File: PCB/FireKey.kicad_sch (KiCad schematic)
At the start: 76 parts, among them P1 Pad, P2 Pad, SW1 SW_MEC_4A, U1 Arduino_Pro_Micro_USB-C

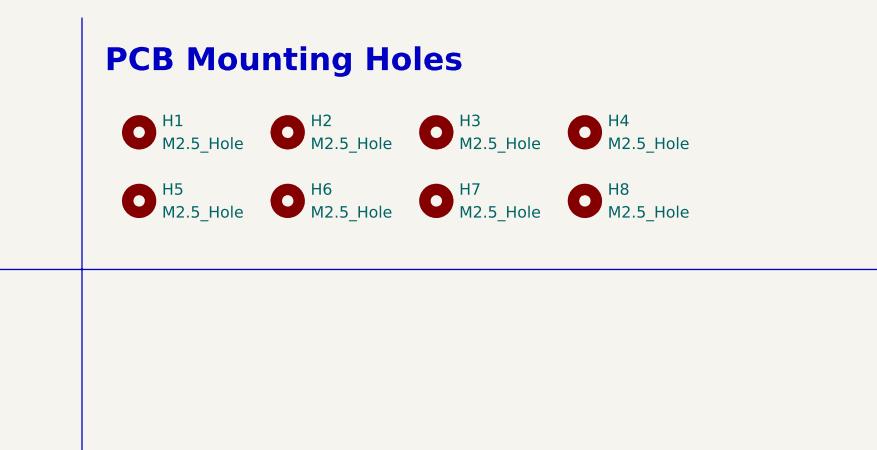
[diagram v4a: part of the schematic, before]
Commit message: deleted unused Mounting Holes in schematic
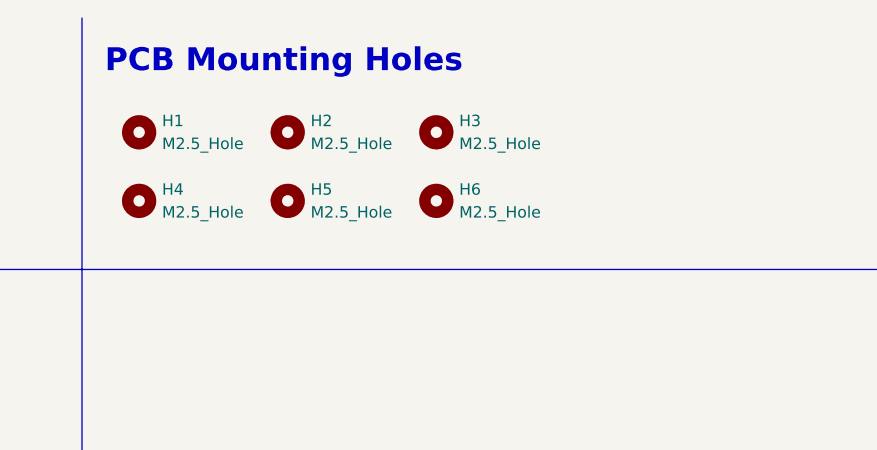
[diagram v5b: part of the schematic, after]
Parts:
- removed H7, H8: M2.5_Hole, MountingHole:MountingHole_2.7mm_M2.5, symbol Mechanical:MountingHole
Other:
- moved on the sheet: H4, H5, H6
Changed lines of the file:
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@@
     (pin "2")
   )
-  (symbol (lib_id "Mechanical:MountingHole") (at 194.31 33.02 0) (unit 1)
+  (symbol (lib_id "Mechanical:MountingHole") (at 210.82 33.02 0) (unit 1)
     (in_bom no) (on_board yes) (fields_autoplaced)
-    (property "Reference" "H5" (id 0) (at 196.85 31.7499 0)
-      (effects (font (size 1.27 1.27)) (justify left))
-    )
-    (property "Value" "M2.5_Hole" (id 1) (at 196.85 34.2899 0)
-      (effects (font (size 1.27 1.27)) (justify left))
-    )
-    (property "Footprint" "MountingHole:MountingHole_2.7mm_M2.5" (id 2) (at 194.31 33.02 0)
-      (effects (font (size 1.27 1.27)) hide)
-    )
-    (property "Datasheet" "-" (id 3) (at 194.31 33.02 0)
-      (effects (font (size 1.27 1.27)) hide)
-    )
-    (property "Part#" "-" (id 4) (at 194.31 33.02 0)
-      (effects (font (size 1.27 1.27)) hide)
-    )
-    (property "Supplier" "-" (id 5) (at 194.31 33.02 0)
+    (property "Reference" "H5" (id 0) (at 213.36 31.7499 0)
+      (effects (font (size 1.27 1.27)) (justify left))
+    )
+    (property "Value" "M2.5_Hole" (id 1) (at 213.36 34.2899 0)
+      (effects (font (size 1.27 1.27)) (justify left))
+    )
+    (property "Footprint" "MountingHole:MountingHole_2.7mm_M2.5" (id 2) (at 210.82 33.02 0)
+      (effects (font (size 1.27 1.27)) hide)
+    )
+    (property "Datasheet" "-" (id 3) (at 210.82 33.02 0)
+      (effects (font (size 1.27 1.27)) hide)
+    )
+    (property "Part#" "-" (id 4) (at 210.82 33.02 0)
+      (effects (font (size 1.27 1.27)) hide)
+    )
+    (property "Supplier" "-" (id 5) (at 210.82 33.02 0)
       (effects (font (size 1.27 1.27)) hide)
     )
@@
     (pin "4")
   )
-  (symbol (lib_id "Mechanical:MountingHole") (at 210.82 33.02 0) (unit 1)
+  (symbol (lib_id "Mechanical:MountingHole") (at 227.33 33.02 0) (unit 1)
     (in_bom no) (on_board yes) (fields_autoplaced)
-    (property "Reference" "H6" (id 0) (at 213.36 31.7499 0)
-      (effects (font (size 1.27 1.27)) (justify left))
-    )
-    (property "Value" "M2.5_Hole" (id 1) (at 213.36 34.2899 0)
-      (effects (font (size 1.27 1.27)) (justify left))
-    )
-    (property "Footprint" "MountingHole:MountingHole_2.7mm_M2.5" (id 2) (at 210.82 33.02 0)
-      (effects (font (size 1.27 1.27)) hide)
-    )
-    (property "Datasheet" "-" (id 3) (at 210.82 33.02 0)
-      (effects (font (size 1.27 1.27)) hide)
-    )
-    (property "Part#" "-" (id 4) (at 210.82 33.02 0)
-      (effects (font (size 1.27 1.27)) hide)
-    )
-    (property "Supplier" "-" (id 5) (at 210.82 33.02 0)
+    (property "Reference" "H6" (id 0) (at 229.87 31.7499 0)
+      (effects (font (size 1.27 1.27)) (justify left))
+    )
+    (property "Value" "M2.5_Hole" (id 1) (at 229.87 34.2899 0)
+      (effects (font (size 1.27 1.27)) (justify left))
+    )
+    (property "Footprint" "MountingHole:MountingHole_2.7mm_M2.5" (id 2) (at 227.33 33.02 0)
+      (effects (font (size 1.27 1.27)) hide)
+    )
+    (property "Datasheet" "-" (id 3) (at 227.33 33.02 0)
+      (effects (font (size 1.27 1.27)) hide)
+    )
+    (property "Part#" "-" (id 4) (at 227.33 33.02 0)
+      (effects (font (size 1.27 1.27)) hide)
+    )
+    (property "Supplier" "-" (id 5) (at 227.33 33.02 0)
       (effects (font (size 1.27 1.27)) hide)
     )
@@
     (pin "4")
   )
-  (symbol (lib_id "Mechanical:MountingHole") (at 227.33 33.02 0) (unit 1)
-    (in_bom no) (on_board yes) (fields_autoplaced)
-    (property "Reference" "H7" (id 0) (at 229.87 31.7499 0)
-      (effects (font (size 1.27 1.27)) (justify left))
-    )
-    (property "Value" "M2.5_Hole" (id 1) (at 229.87 34.2899 0)
-      (effects (font (size 1.27 1.27)) (justify left))
-    )
-    (property "Footprint" "MountingHole:MountingHole_2.7mm_M2.5" (id 2) (at 227.33 33.02 0)
-      (effects (font (size 1.27 1.27)) hide)
-    )
-    (property "Datasheet" "-" (id 3) (at 227.33 33.02 0)
-      (effects (font (size 1.27 1.27)) hide)
-    )
-    (property "Part#" "-" (id 4) (at 227.33 33.02 0)
-      (effects (font (size 1.27 1.27)) hide)
-    )
-    (property "Supplier" "-" (id 5) (at 227.33 33.02 0)
-      (effects (font (size 1.27 1.27)) hide)
-    )
-  )
   (symbol (lib_id "power:GND") (at 171.45 59.69 180) (unit 1)
     (in_bom yes) (on_board yes)
@@
     (pin "1")
   )
-  (symbol (lib_id "Mechanical:MountingHole") (at 243.84 25.4 0) (unit 1)
+  (symbol (lib_id "Mechanical:MountingHole") (at 194.31 33.02 0) (unit 1)
     (in_bom no) (on_board yes) (fields_autoplaced)
-    (property "Reference" "H4" (id 0) (at 246.38 24.1299 0)
-      (effects (font (size 1.27 1.27)) (justify left))
-    )
-    (property "Value" "M2.5_Hole" (id 1) (at 246.38 26.6699 0)
-      (effects (font (size 1.27 1.27)) (justify left))
-    )
-    (property "Footprint" "MountingHole:MountingHole_2.7mm_M2.5" (id 2) (at 243.84 25.4 0)
-      (effects (font (size 1.27 1.27)) hide)
-    )
-    (property "Datasheet" "-" (id 3) (at 243.84 25.4 0)
-      (effects (font (size 1.27 1.27)) hide)
-    )
-    (property "Part#" "-" (id 4) (at 243.84 25.4 0)
-      (effects (font (size 1.27 1.27)) hide)
-    )
-    (property "Supplier" "-" (id 5) (at 243.84 25.4 0)
+    (property "Reference" "H4" (id 0) (at 196.85 31.7499 0)
+      (effects (font (size 1.27 1.27)) (justify left))
+    )
+    (property "Value" "M2.5_Hole" (id 1) (at 196.85 34.2899 0)
+      (effects (font (size 1.27 1.27)) (justify left))
+    )
+    (property "Footprint" "MountingHole:MountingHole_2.7mm_M2.5" (id 2) (at 194.31 33.02 0)
+      (effects (font (size 1.27 1.27)) hide)
+    )
+    (property "Datasheet" "-" (id 3) (at 194.31 33.02 0)
+      (effects (font (size 1.27 1.27)) hide)
+    )
+    (property "Part#" "-" (id 4) (at 194.31 33.02 0)
+      (effects (font (size 1.27 1.27)) hide)
+    )
+    (property "Supplier" "-" (id 5) (at 194.31 33.02 0)
       (effects (font (size 1.27 1.27)) hide)
     )
@@
     (pin "2")
   )
-  (symbol (lib_id "Mechanical:MountingHole") (at 243.84 33.02 0) (unit 1)
-    (in_bom no) (on_board yes) (fields_autoplaced)
-    (property "Reference" "H8" (id 0) (at 246.38 31.7499 0)
-      (effects (font (size 1.27 1.27)) (justify left))
-    )
-    (property "Value" "M2.5_Hole" (id 1) (at 246.38 34.2899 0)
-      (effects (font (size 1.27 1.27)) (justify left))
-    )
-    (property "Footprint" "MountingHole:MountingHole_2.7mm_M2.5" (id 2) (at 243.84 33.02 0)
-      (effects (font (size 1.27 1.27)) hide)
-    )
-    (property "Datasheet" "-" (id 3) (at 243.84 33.02 0)
-      (effects (font (size 1.27 1.27)) hide)
-    )
-    (property "Part#" "-" (id 4) (at 243.84 33.02 0)
-      (effects (font (size 1.27 1.27)) hide)
-    )
-    (property "Supplier" "-" (id 5) (at 243.84 33.02 0)
-      (effects (font (size 1.27 1.27)) hide)
-    )
-  )
   (sheet_instances
     (path "/" (page "1"))
@@
       (reference "H6") (unit 1) (value "M2.5_Hole") (footprint "MountingHole:MountingHole_2.7mm_M2.5")
     )
-    (path "/8ab241e9-fc3a-4e73-81b5-b360d79d2a92"
-      (reference "H7") (unit 1) (value "M2.5_Hole") (footprint "MountingHole:MountingHole_2.7mm_M2.5")
-    )
-    (path "/ff3e174f-a970-44ce-b4d8-5c37d2b3d8dc"
-      (reference "H8") (unit 1) (value "M2.5_Hole") (footprint "MountingHole:MountingHole_2.7mm_M2.5")
-    )
     (path "/11379805-2b0d-4db7-8cef-30119ba5698b"

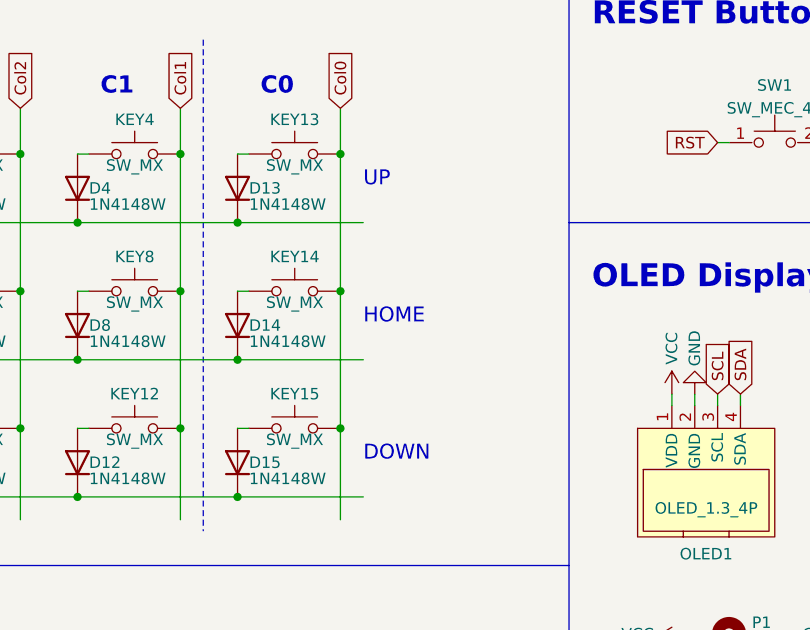
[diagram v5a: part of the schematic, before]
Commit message: updated key labels in schematic
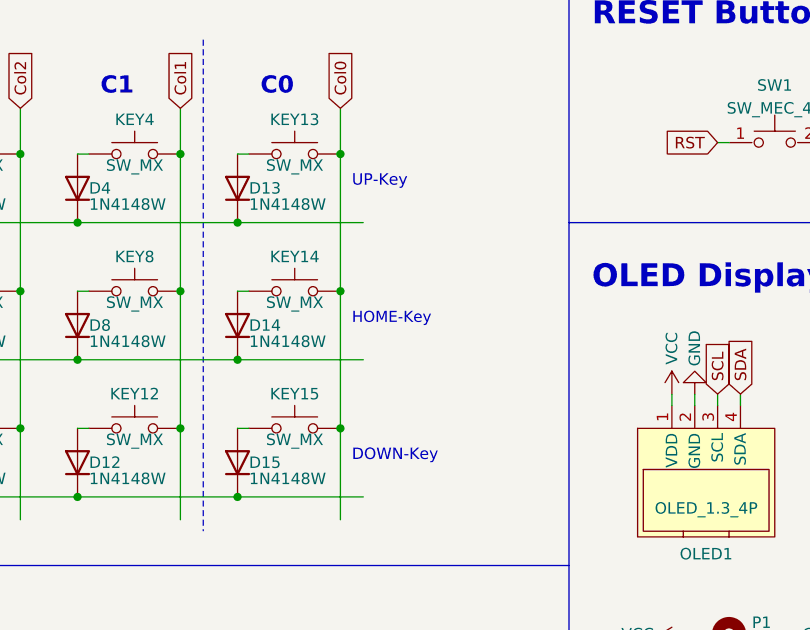
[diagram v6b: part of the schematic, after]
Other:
- note added: "DOWN-Key"
- note added: "HOME-Key"
- note added: "UP-Key"
- note removed: "DOWN"
- note removed: "HOME"
- note removed: "UP"
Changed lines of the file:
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@@
     (effects (font (size 2.54 2.54) bold) (justify left bottom))
   )
-  (text "DOWN" (at 114.3 67.31 0)
-    (effects (font (size 1.651 1.651)) (justify left bottom))
+  (text "DOWN-Key" (at 113.03 67.31 0)
+    (effects (font (size 1.27 1.27)) (justify left bottom))
   )
-  (text "UP" (at 114.3 36.83 0)
-    (effects (font (size 1.651 1.651)) (justify left bottom))
+  (text "UP-Key" (at 113.03 36.83 0)
+    (effects (font (size 1.27 1.27)) (justify left bottom))
   )
   (text "LED Strip" (at 15.24 85.09 0)
     (effects (font (size 2.54 2.54) bold) (justify left bottom))
   )
-  (text "HOME" (at 114.3 52.07 0)
-    (effects (font (size 1.651 1.651)) (justify left bottom))
+  (text "HOME-Key" (at 113.03 52.07 0)
+    (effects (font (size 1.227 1.227)) (justify left bottom))
   )
   (text "C0" (at 102.87 26.67 0)
